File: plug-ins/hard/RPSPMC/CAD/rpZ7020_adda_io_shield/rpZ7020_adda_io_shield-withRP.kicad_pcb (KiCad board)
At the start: 4 copper layers, 70.6 x 94.5 mm, 38 parts, among them J1 Samtec_ASP-134486-01, J2 Conn_01x03_Socket, J2-FMC-RP1 Conn_02x20, J3-FMC-POWER1 Conn_02x06_Odd_Even, J4-FMC-AUX1 Conn_02x06_Odd_Even

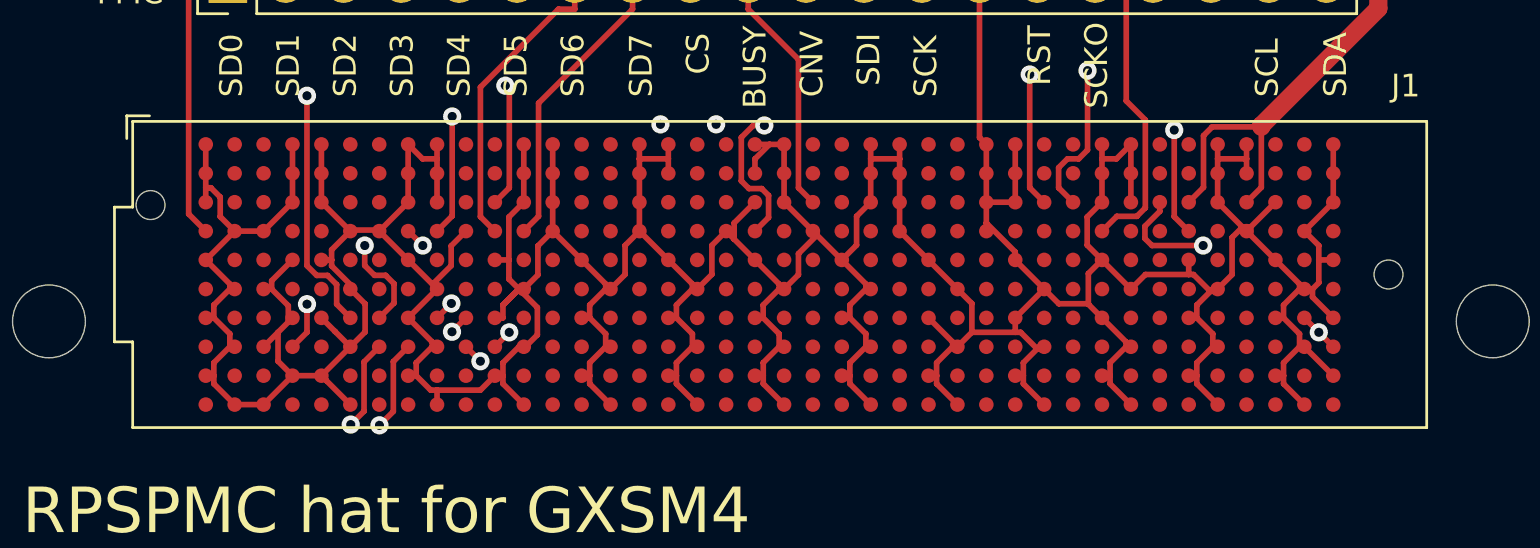
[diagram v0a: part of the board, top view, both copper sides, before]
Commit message: updated 3d model
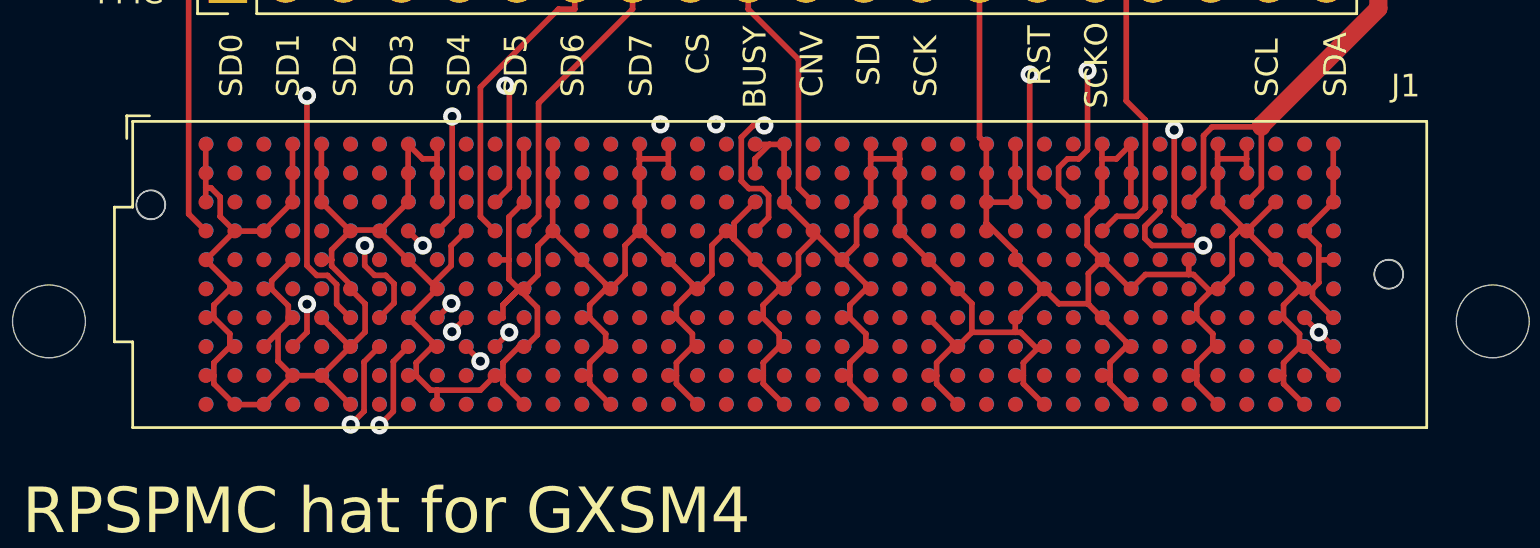
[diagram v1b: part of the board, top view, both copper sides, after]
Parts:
- added REF**: Samtec_FMC_ASP-134602-01_10x40_P1.27mm_Vertical, Connector_Samtec:Samtec_FMC_ASP-134602-01_10x40_P1.27mm_Vertical, B.Cu at (149.0, 148.1)

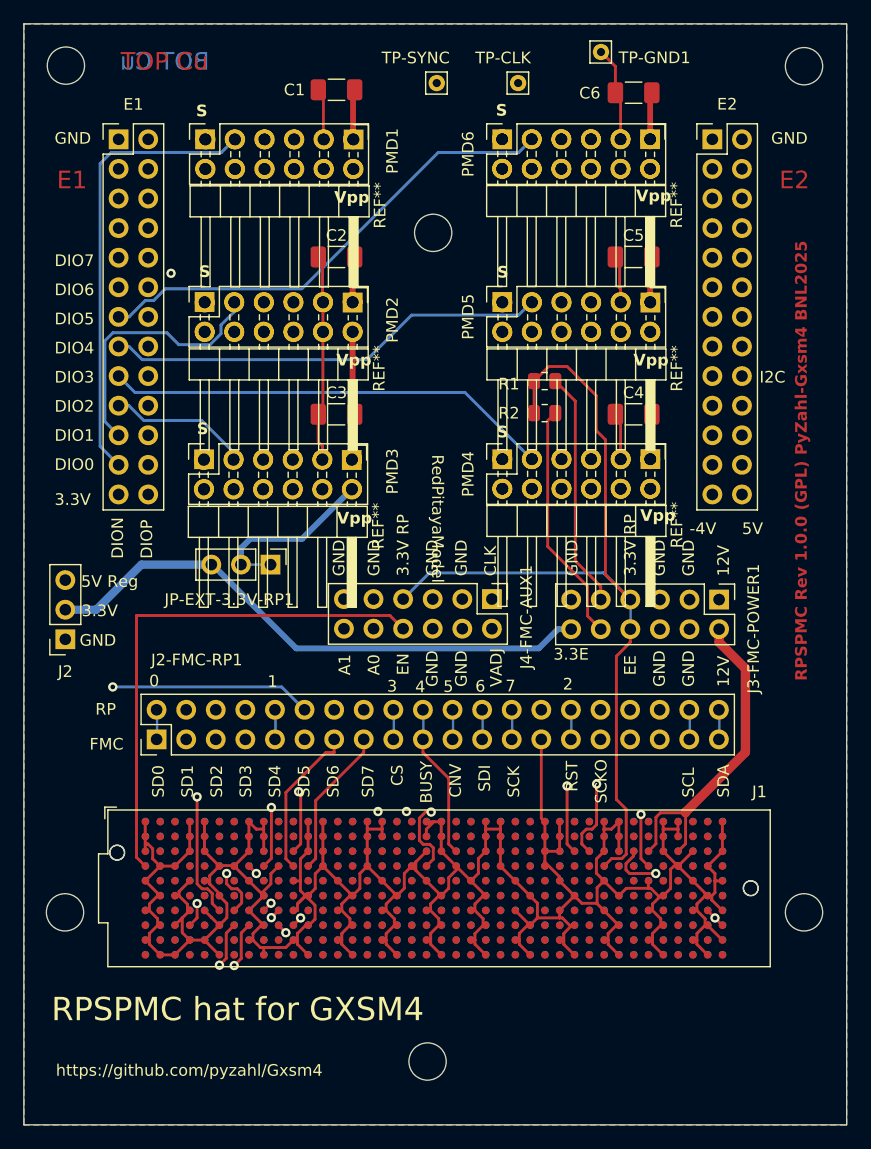
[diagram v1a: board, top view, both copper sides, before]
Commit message: added 3d models
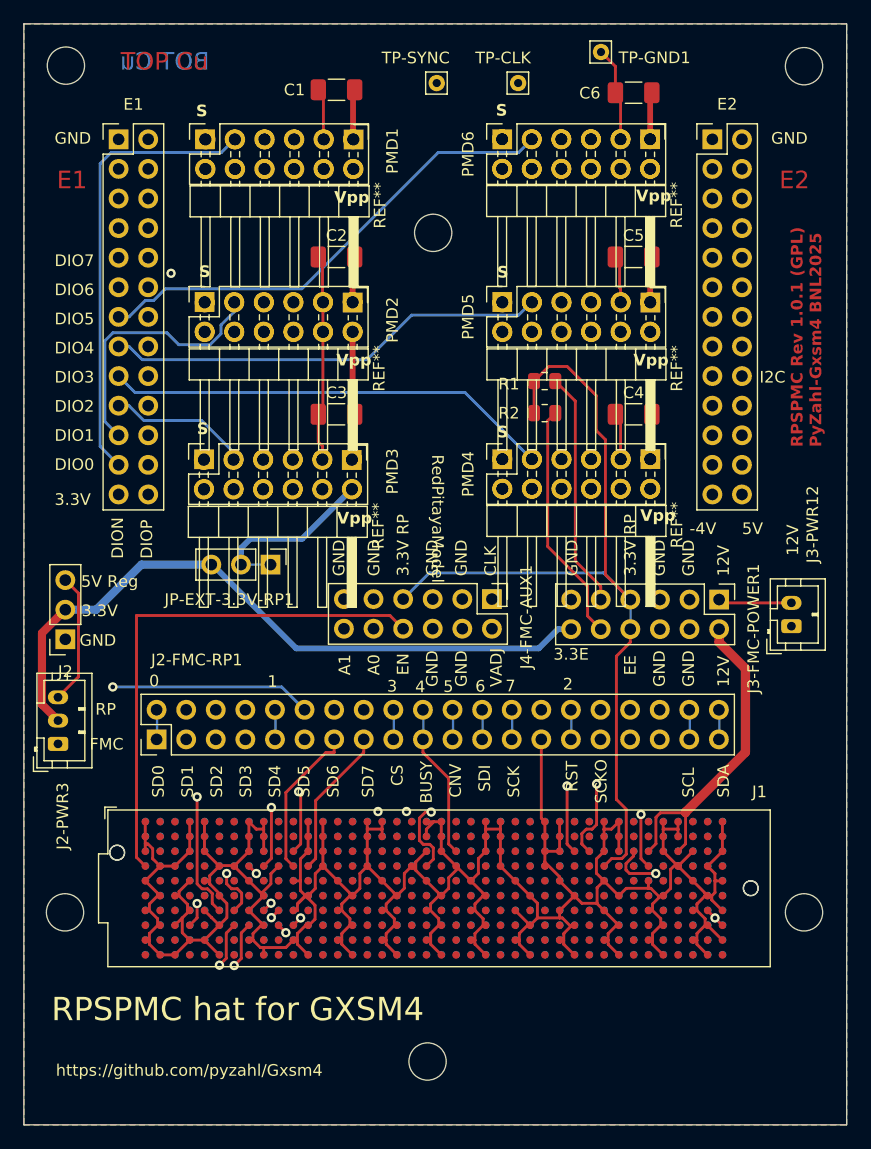
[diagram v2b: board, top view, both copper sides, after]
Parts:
- added J2-PWR3: Conn_01x03_Pin, Connector_JST:JST_PH_B3B-PH-K_1x03_P2.00mm_Vertical, F.Cu at (116.7, 135.7)
- added J3-PWR12: Conn_01x02_Pin, Connector_JST:JST_PH_B2B-PH-K_1x02_P2.00mm_Vertical, F.Cu at (179.7, 125.6)
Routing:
- net 5V USB: track 0.00 -> 11.2 mm
- net EXT 3.3V DAC: track 48.8 -> 59.7 mm
- net +12V FMC: track 30.7 -> 37.0 mm
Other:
- board text added: "RPSPMC Rev 1.0.1 (GPL) PyZahl-Gxsm4 BNL2025"
- board text removed: "RPSPMC Rev 1.0.0 (GPL) PyZahl-Gxsm4 BNL2025"
